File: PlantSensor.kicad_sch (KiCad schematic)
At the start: 51 parts, among them J1 SCREW-TERMINAL-GREEN_2P-5.0_, J2 SCREW-TERMINAL-GREEN_2P-5.0_, J3 SCREW-TERMINAL-GREEN_2P-5.0_, J4 SCREW-TERMINAL-GREEN_2P-5.0_, J5 DIP-BLACK-MALE-HEADER-VERT_2P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, J6 DIP-BLACK-MALE-HEADER-VERT_4P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, Q1 N-Channel_30-V_MOSFET, Q2 N-Channel_30-V_MOSFET, Q3 N-Channel_30-V_MOSFET, Q4 N-Channel_30-V_MOSFET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

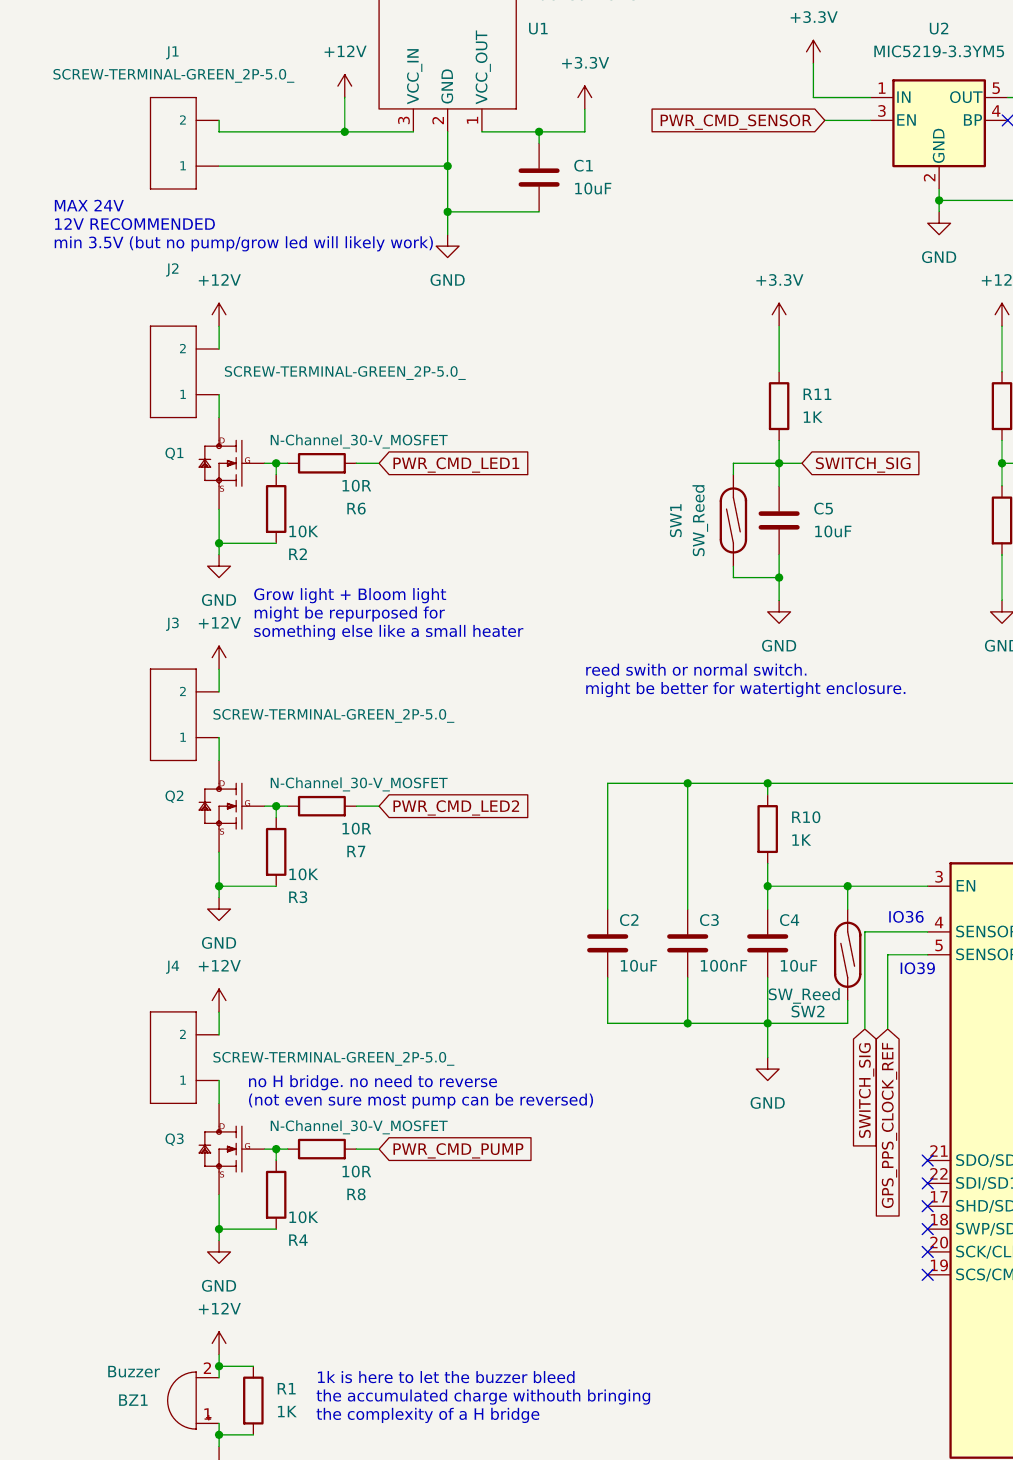
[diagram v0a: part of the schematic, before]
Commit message: fixed trace size + diode to prevent inductive load from damaging the mosfet
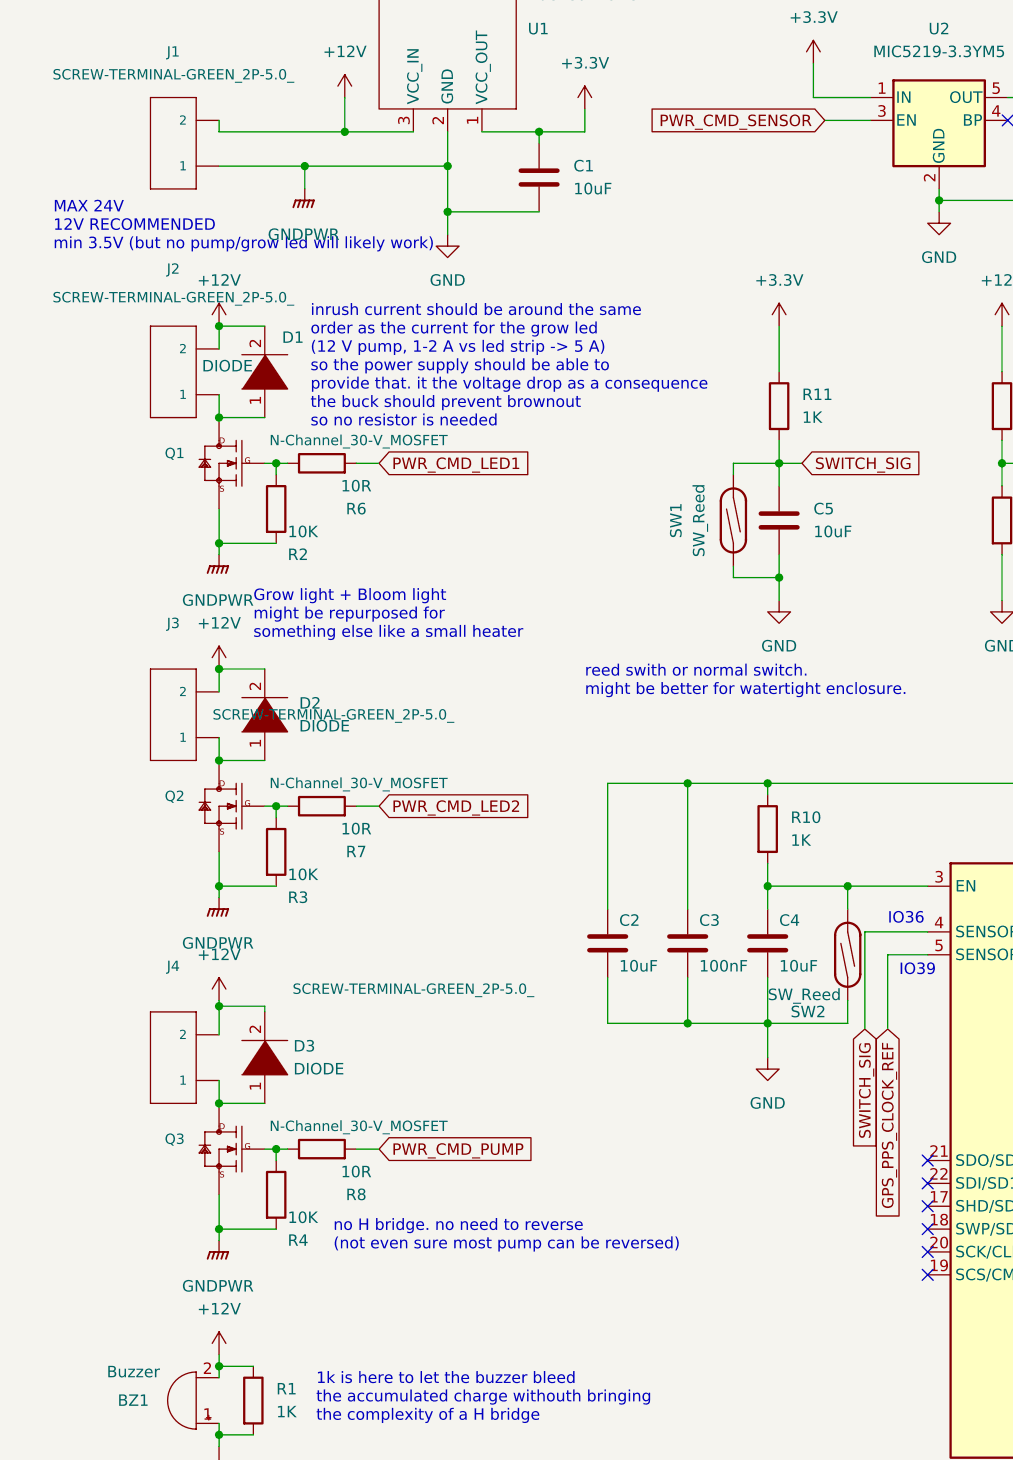
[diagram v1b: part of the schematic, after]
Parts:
- added D1, D2, D3: DIODE, Diode_SMD:D_SOD-123, symbol pspice:DIODE
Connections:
- net +12V: now also D1.2 (A), D2.2 (A), D3.2 (A)
- net at J2.1, Q1.3 (D): now also D1.1 (K)
- net at J3.1, Q2.3 (D): now also D2.1 (K)
- net at J4.1, Q3.3 (D): now also D3.1 (K)
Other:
- note added: "inrush current should be around the same order as the current for the grow led (12 V pump, 1-2 A vs led strip -> 5 A) so the power supply should be able to provide that. it the voltage drop as a consequence the buck should prevent brownout so no resistor is needed"

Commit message: small improuvment
added mounting hole
improved silk screen
generated gerber for manufacturing
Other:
- company: (none) -> Aperture Science
- title: (none) -> PlantSensor
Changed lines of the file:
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@@
 (kicad_sch (version 20211123) (generator eeschema)
   (paper "A4")
+  (title_block
+    (title "PlantSensor")
+    (date "2022-06-19")
+    (rev "3")
+    (company "Aperture Science")
+    (comment 1 "Author : Nathann Morand")
+  )
   (junction (at 33.02 175.26) (diameter 0) (color 0 0 0 0)
   )
